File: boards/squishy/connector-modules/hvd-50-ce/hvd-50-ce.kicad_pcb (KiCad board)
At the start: 6 copper layers, 75 x 34 mm, 20 parts, among them J1 SCSI PHY Mezz, J3 Conn_01x04, J5 Centronics 50, U1 M24C02-RMC

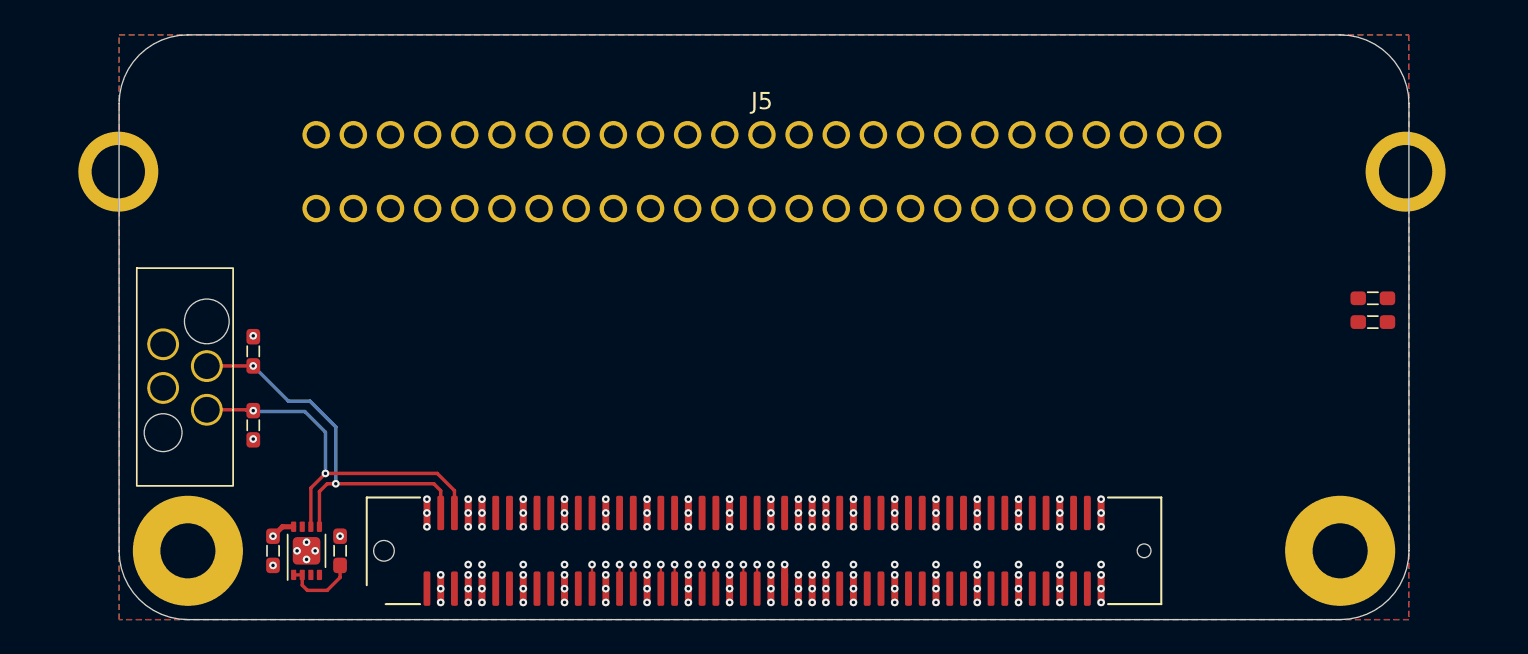
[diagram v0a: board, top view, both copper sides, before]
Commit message: squishy: connectors: added little earbs to the hvd-50-ce connector board
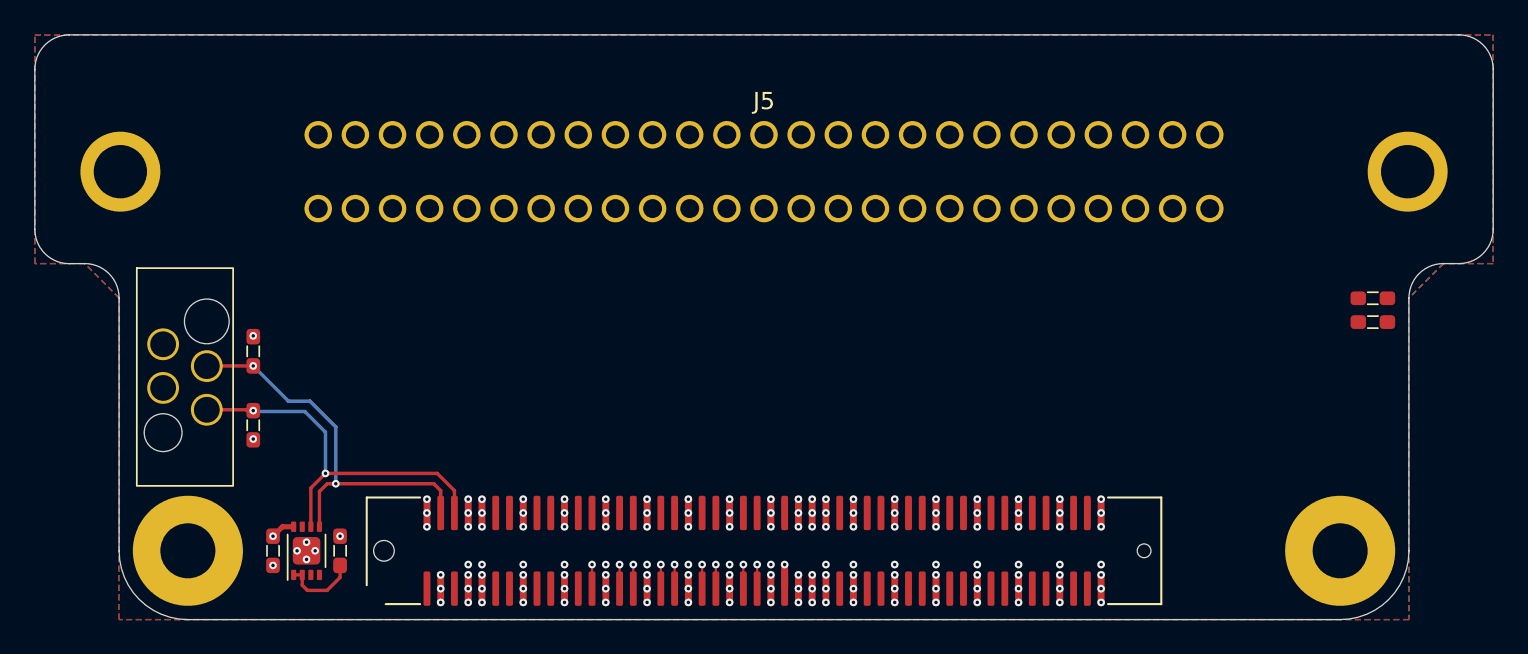
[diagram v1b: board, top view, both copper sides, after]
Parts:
- moved J5 0.12 mm to (147.5, 114.0)
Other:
- board size 75 x 34 mm -> 84.8 x 34 mm
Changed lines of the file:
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@@
 	(footprint "lethalbit-connectors:112-050-213R001"
 		(layer "F.Cu")
-		(at 147.38 113.955 180)
+		(at 147.5 113.955 180)
 		(descr "Norcomp 50-pin Centronics Connector")
 		(property "Reference" "J5"
@@
 	)
 	(gr_line
-		(start 181 106)
-		(end 114 106)
+		(start 187.9 106)
+		(end 107.1 106)
 		(locked yes)
 		(stroke
@@
 	)
 	(gr_arc
-		(start 110 110)
-		(mid 111.171573 107.171573)
-		(end 114 106)
+		(start 107.997502 119.297502)
+		(mid 109.413482 119.88402)
+		(end 110 121.3)
+		(locked yes)
+		(stroke
+			(width 0.05)
+			(type default)
+		)
+		(layer "Edge.Cuts")
+	)
+	(gr_line
+		(start 187 119.3)
+		(end 187.9 119.3)
 		(locked yes)
 		(stroke
@@
 	(gr_line
 		(start 185 136)
-		(end 185 110)
+		(end 185 121.3)
 		(locked yes)
 		(stroke
@@
 	)
 	(gr_arc
-		(start 181 106)
-		(mid 183.828427 107.171573)
-		(end 185 110)
+		(start 105.1 108.002498)
+		(mid 105.686517 106.586517)
+		(end 107.102498 106)
+		(locked yes)
+		(stroke
+			(width 0.05)
+			(type default)
+		)
+		(layer "Edge.Cuts")
+	)
+	(gr_arc
+		(start 107.102498 119.304996)
+		(mid 105.686517 118.718479)
+		(end 105.1 117.302498)
+		(locked yes)
+		(stroke
+			(width 0.05)
+			(type default)
+		)
+		(layer "Edge.Cuts")
+	)
+	(gr_arc
+		(start 185 121.3)
+		(mid 185.586518 119.88402)
+		(end 187.002498 119.297502)
 		(locked yes)
 		(stroke
@@
 	(gr_line
 		(start 110 136)
-		(end 110 110)
+		(end 110 121.3)
+		(locked yes)
+		(stroke
+			(width 0.05)
+			(type default)
+		)
+		(layer "Edge.Cuts")
+	)
+	(gr_line
+		(start 108 119.302498)
+		(end 107.1 119.302498)
+		(locked yes)
+		(stroke
+			(width 0.05)
+			(type default)
+		)
+		(layer "Edge.Cuts")
+	)
+	(gr_arc
+		(start 189.9 117.3)
+		(mid 189.313482 118.715981)
+		(end 187.897502 119.302498)
 		(locked yes)
 		(stroke
@@
 		(layer "Edge.Cuts")
 	)
+	(gr_arc
+		(start 187.897502 105.997502)
+		(mid 189.313483 106.584019)
+		(end 189.9 108)
+		(locked yes)
+		(stroke
+			(width 0.05)
+			(type default)
+		)
+		(layer "Edge.Cuts")
+	)
+	(gr_line
+		(start 189.9 117.3)
+		(end 189.9 108)
+		(locked yes)
+		(stroke
+			(width 0.05)
+			(type default)
+		)
+		(layer "Edge.Cuts")
+	)
+	(gr_line
+		(start 105.1 117.302498)
+		(end 105.1 108.002498)
+		(locked yes)
+		(stroke
+			(width 0.05)
+			(type default)
+		)
+		(layer "Edge.Cuts")
+	)
 	(gr_line
 		(start 23.5 34.517209)
@@
 		(polygon
 			(pts
-				(xy 185 140) (xy 110 140) (xy 110 106) (xy 185 106)
+				(xy 189.9 119.3) (xy 187 119.3) (xy 185 121.3) (xy 185 140) (xy 110 140) (xy 110 121.3) (xy 108 119.3)
+				(xy 105.1 119.3) (xy 105.1 106) (xy 189.9 106)
 			)
 		)
@@
 		(polygon
 			(pts
-				(xy 110 140) (xy 185 140) (xy 185 106) (xy 110 106)
+				(xy 105.1 119.3) (xy 108 119.3) (xy 110 121.3) (xy 110 140) (xy 185 140) (xy 185 121.3) (xy 187 119.3)
+				(xy 189.9 119.3) (xy 189.9 106) (xy 105.1 106)
 			)
 		)

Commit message: squishy: connectors: started routing on the hvd-50-ce
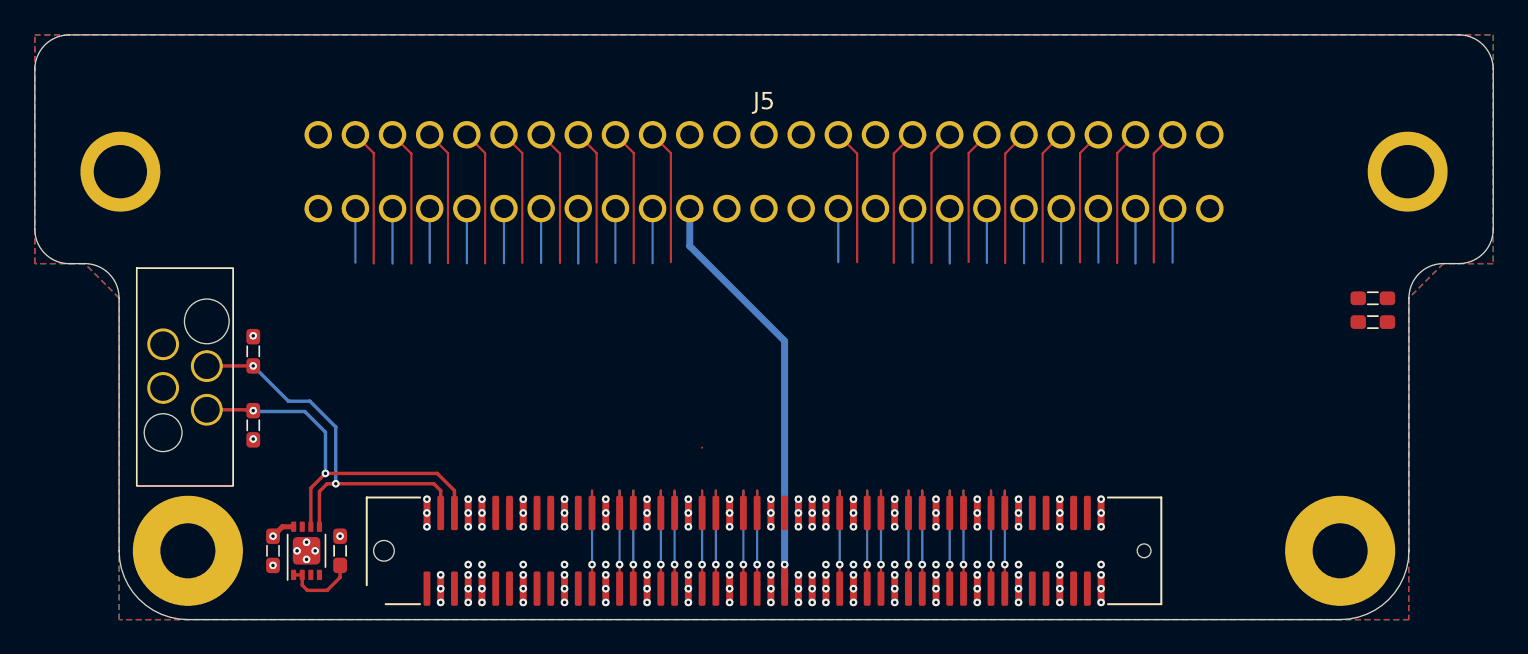
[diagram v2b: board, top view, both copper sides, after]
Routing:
- net /CON.DIFFSENSE: track 1.40 -> 24.4 mm
- net /CON.DB1-: track 0.00 -> 9.24 mm
- net /CON.DB0-: track 0.00 -> 9.23 mm
- net /CON.MSG-: track 0.00 -> 9.22 mm
- net /CON.DB3-: track 0.00 -> 9.21 mm
- net /CON.DB5-: track 0.00 -> 9.21 mm
- net /CON.DB2-: track 0.00 -> 9.21 mm
- net /CON.DB7-: track 0.00 -> 9.21 mm
- net /CON.BSY-: track 0.00 -> 9.20 mm
- net /CON.REQ-: track 0.00 -> 9.19 mm
- net /CON.ACK-: track 0.00 -> 9.19 mm
- net /CON.DB4-: track 0.00 -> 9.19 mm
- net /CON.I/O-: track 0.00 -> 9.18 mm
- net /CON.DB6-: track 0.00 -> 9.17 mm
- net /CON.ATN-: track 0.00 -> 9.16 mm
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
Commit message: squishy: connectors: Roughly routed out the hd-50-ce connector, still needs wiggles
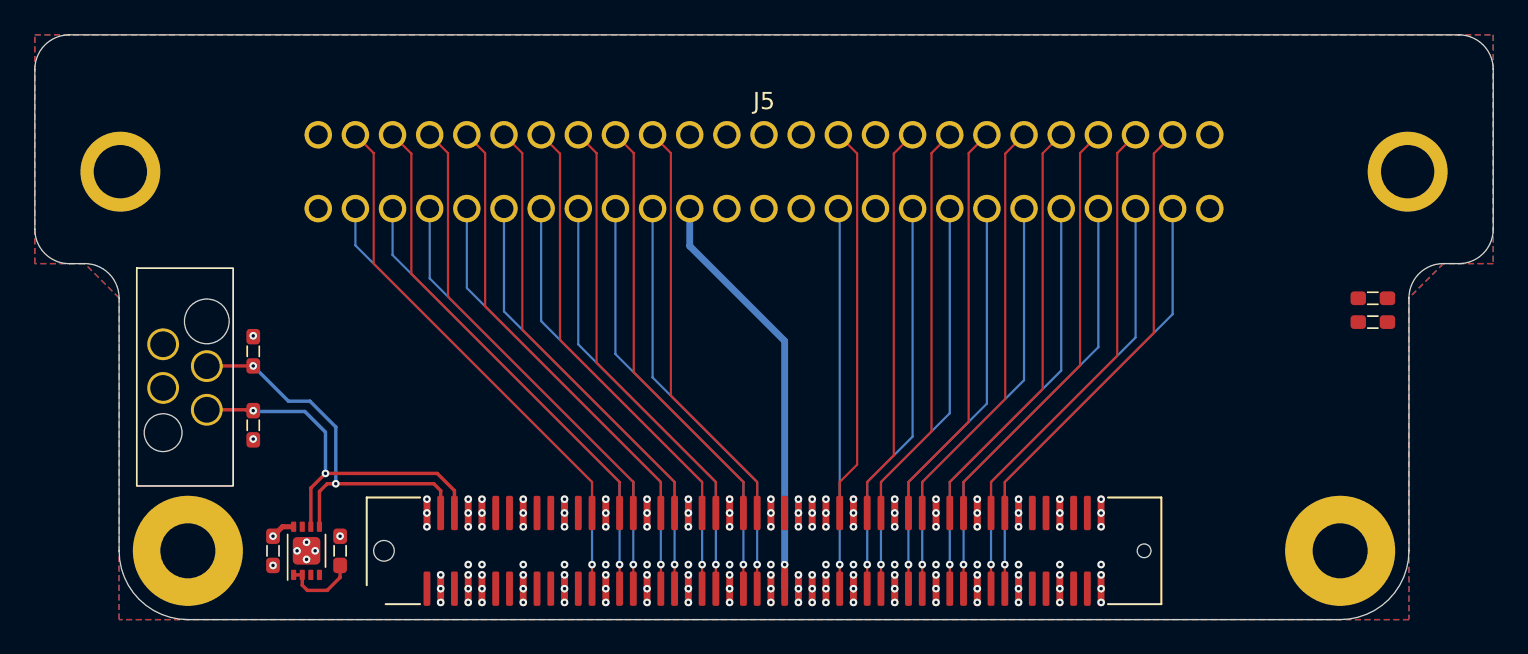
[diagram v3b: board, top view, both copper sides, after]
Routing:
- net /CON.DB0+: track 8.84 -> 27.8 mm
- net /CON.DB1+: track 8.90 -> 27.6 mm
- net /CON.DB0-: track 9.23 -> 27.7 mm
- net /CON.DB1-: track 9.24 -> 27.5 mm
- net /CON.DB2+: track 8.86 -> 27.0 mm
- net /CON.DB3+: track 8.88 -> 26.8 mm
- net /CON.DB2-: track 9.21 -> 26.9 mm
- net /CON.DB3-: track 9.21 -> 26.7 mm
- net /CON.DB4+: track 8.88 -> 26.2 mm
- net /CON.I/O+: track 8.84 -> 26.1 mm
- net /CON.DB5+: track 8.86 -> 26.0 mm
- net /CON.DB4-: track 9.19 -> 26.1 mm
- net /CON.I/O-: track 9.18 -> 26.0 mm
- net /CON.REQ+: track 8.90 -> 25.6 mm
- net /CON.DB5-: track 9.21 -> 25.9 mm
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
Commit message: squishy: connectors: added shield cap/resistor to hd-50-ce
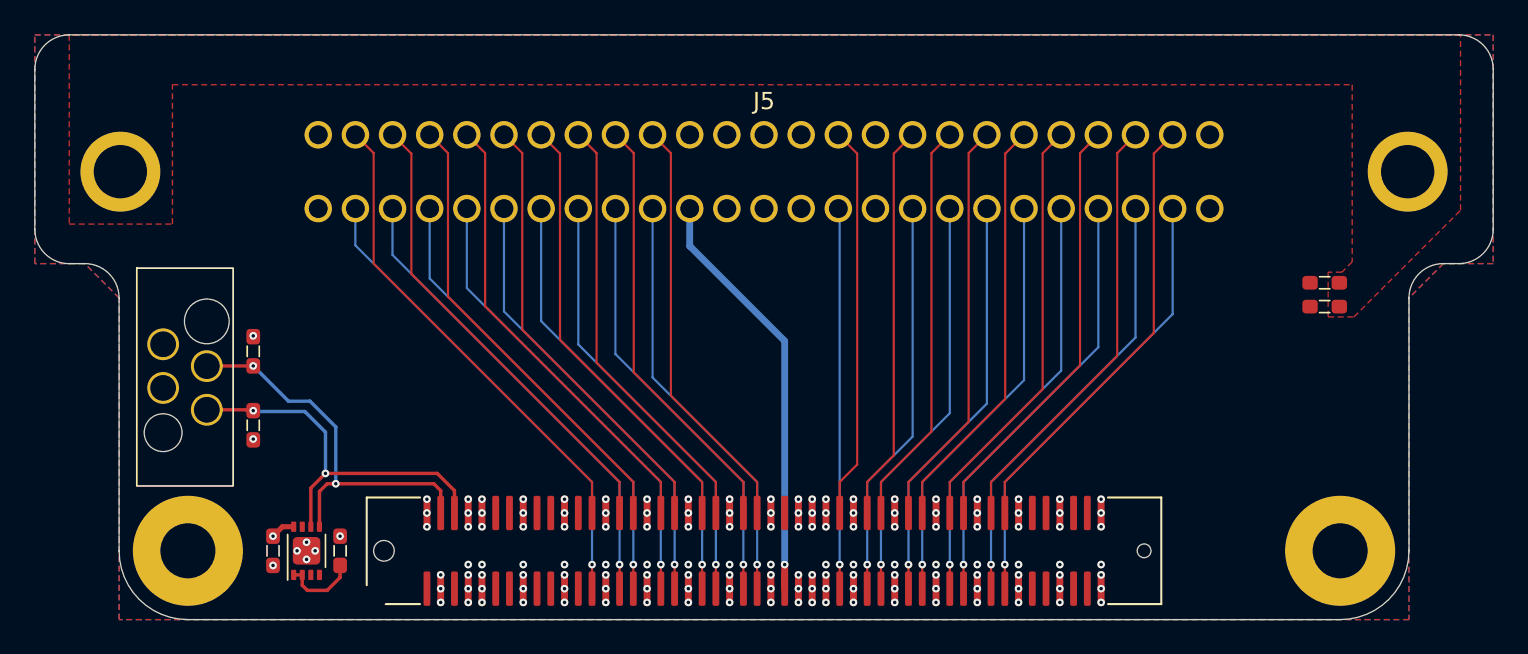
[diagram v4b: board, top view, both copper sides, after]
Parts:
- moved C2 3.61 mm to (180.1, 120.4), turned to 180 degrees
- moved R4 2.84 mm to (180.1, 121.8), turned to 0 degrees
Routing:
- added copper zone on F.Cu, net Net-(C2-Pad1)
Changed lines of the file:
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@@
 	(footprint "rhais_rcl:R0603"
 		(layer "F.Cu")
-		(at 182.9 121.315 180)
+		(at 180.1 121.8)
 		(descr "Ceramic Chip Resistor, 0603 (1608 metric) iron and air reflow solderable")
 		(property "Reference" "R4"
-			(at 0 1.315 0)
+			(at 0 1.314999 0)
 			(layer "F.Fab")
 			(effects
@@
 		)
 		(property "MFR" ""
-			(at 0 0 180)
+			(at 0 0 0)
 			(unlocked yes)
 			(layer "F.Fab")
@@
 		)
 		(property "MPN" ""
-			(at 0 0 180)
+			(at 0 0 0)
 			(unlocked yes)
 			(layer "F.Fab")
@@
 		)
 		(property "Tolerance" ""
-			(at 0 0 180)
+			(at 0 0 0)
 			(unlocked yes)
 			(layer "F.Fab")
@@
 		)
 		(property "SUPPLIER" "DigiKey"
-			(at 0 0 180)
+			(at 0 0 0)
 			(unlocked yes)
 			(layer "F.Fab")
@@
 		)
 		(property "SUPPLIER_OC" ""
-			(at 0 0 180)
+			(at 0 0 0)
 			(unlocked yes)
 			(layer "F.Fab")
@@
 		)
 		(property "SUPPLIER_URL" ""
-			(at 0 0 180)
+			(at 0 0 0)
 			(unlocked yes)
 			(layer "F.Fab")
@@
 		)
 		(fp_line
-			(start 0.3 -0.349999)
-			(end -0.3 -0.349999)
+			(start -0.3 0.349999)
+			(end 0.3 0.349999)
 			(stroke
 				(width 0.1)
@@
 		)
 		(fp_line
-			(start -0.3 0.349999)
-			(end 0.3 0.349999)
+			(start 0.3 -0.349999)
+			(end -0.3 -0.349999)
 			(stroke
 				(width 0.1)
@@
 		)
 		(fp_line
-			(start 1.55 0.65)
-			(end -1.55 0.65)
+			(start -1.55 -0.65)
+			(end 1.55 -0.65)
 			(stroke
 				(width 0.05)
@@
 		)
 		(fp_line
-			(start 1.55 -0.65)
-			(end 1.55 0.65)
+			(start -1.55 0.65)
+			(end -1.55 -0.65)
 			(stroke
 				(width 0.05)
@@
 		)
 		(fp_line
-			(start -1.55 0.65)
-			(end -1.55 -0.65)
+			(start 1.55 -0.65)
+			(end 1.55 0.65)
 			(stroke
 				(width 0.05)
@@
 		)
 		(fp_line
-			(start -1.55 -0.65)
-			(end 1.55 -0.65)
+			(start 1.55 0.65)
+			(end -1.55 0.65)
 			(stroke
 				(width 0.05)
@@
 		)
 		(fp_line
-			(start 0.45 -0.349999)
-			(end -0.45 -0.349999)
+			(start -0.45 0.349999)
+			(end 0.45 0.349999)
 			(stroke
 				(width 0.1)
@@
 		)
 		(fp_line
-			(start -0.45 0.349999)
-			(end 0.45 0.349999)
+			(start 0.45 -0.349999)
+			(end -0.45 -0.349999)
 			(stroke
 				(width 0.1)
@@
 		(fp_poly
 			(pts
-				(xy 0.4 0.4) (xy 0.8 0.4) (xy 0.8 -0.4) (xy 0.4 -0.4)
+				(xy -0.8 0.4) (xy -0.4 0.4) (xy -0.4 -0.4) (xy -0.8 -0.4)
 			)
 			(stroke
@@
 		(fp_poly
 			(pts
-				(xy -0.8 0.4) (xy -0.4 0.4) (xy -0.4 -0.4) (xy -0.8 -0.4)
+				(xy 0.4 0.4) (xy 0.8 0.4) (xy 0.8 -0.4) (xy 0.4 -0.4)
 			)
 			(stroke
@@
 		)
 		(pad "1" smd roundrect
-			(at -0.85 0 180)
+			(at -0.85 0)
 			(size 0.9 0.8)
 			(layers "F.Cu" "F.Paste" "F.Mask")
@@
 		)
 		(pad "2" smd roundrect
-			(at 0.85 0 180)
+			(at 0.85 0)
 			(size 0.9 0.8)
 			(layers "F.Cu" "F.Paste" "F.Mask")
@@
 	)
 	(footprint "lethalbit-connectors:112-050-213R001"
+		(locked yes)
 		(layer "F.Cu")
 		(at 147.5 113.955 180)
@@
 	(footprint "rhais_rcl:C0603"
 		(layer "F.Cu")
-		(at 182.9 122.7)
+		(at 180.1 120.415 180)
 		(descr "Multi-Layer Ceramic Chip Capacitor, 0603 (1608 metric) iron and air reflow solderable")
 		(property "Reference" "C2"
@@
 		)
 		(property "MFR" "KEMET"
-			(at 0 0 0)
+			(at 0 0 180)
 			(unlocked yes)
 			(layer "F.Fab")
@@
 		)
 		(property "MPN" "C0603C104M5RACTU"
-			(at 0 0 0)
+			(at 0 0 180)
 			(unlocked yes)
 			(layer "F.Fab")
@@
 		)
 		(property "Tolerance" "±20% 50V"
-			(at 0 0 0)
+			(at 0 0 180)
 			(unlocked yes)
 			(layer "F.Fab")
@@
 		)
 		(property "SUPPLIER" "DigiKey"
-			(at 0 0 0)
+			(at 0 0 180)
 			(unlocked yes)
 			(layer "F.Fab")
@@
 		)
 		(property "SUPPLIER_OC" "399-C0603C104M5RAC7867DKR-ND"
-			(at 0 0 0)
+			(at 0 0 180)
 			(unlocked yes)
 			(layer "F.Fab")
@@
 		)
 		(property "SUPPLIER_URL" "https://www.digikey.com/short/8nqzrr4b"
-			(at 0 0 0)
+			(at 0 0 180)
 			(unlocked yes)
 			(layer "F.Fab")
@@
 		)
 		(fp_line
-			(start -0.3 -0.349999)
-			(end 0.3 -0.349999)
+			(start 0.3 0.349999)
+			(end -0.3 0.349999)
 			(stroke
 				(width 0.1)
@@
 		)
 		(fp_line
-			(start 0.3 0.349999)
-			(end -0.3 0.349999)
+			(start -0.3 -0.349999)
+			(end 0.3 -0.349999)
 			(stroke
 				(width 0.1)
@@
 		)
 		(fp_line
-			(start -1.55 -0.65)
-			(end -1.55 0.65)
+			(start 1.55 0.65)
+			(end 1.55 -0.65)
 			(stroke
 				(width 0.05)
@@
 		)
 		(fp_line
-			(start -1.55 0.65)
-			(end 1.55 0.65)
+			(start 1.55 -0.65)
+			(end -1.55 -0.65)
 			(stroke
 				(width 0.05)
@@
 		)
 		(fp_line
-			(start 1.55 -0.65)
-			(end -1.55 -0.65)
+			(start -1.55 0.65)
+			(end 1.55 0.65)
 			(stroke
 				(width 0.05)
@@
 		)
 		(fp_line
-			(start 1.55 0.65)
-			(end 1.55 -0.65)
+			(start -1.55 -0.65)
+			(end -1.55 0.65)
 			(stroke
 				(width 0.05)
@@
 		)
 		(fp_line
-			(start -0.45 -0.349999)
-			(end 0.45 -0.349999)
+			(start -0.45 0.349999)
+			(end 0.45 0.349999)
 			(stroke
 				(width 0.1)
@@
 		)
 		(fp_line
-			(start -0.45 0.349999)
-			(end 0.45 0.349999)
+			(start -0.45 -0.349999)
+			(end 0.45 -0.349999)
 			(stroke
 				(width 0.1)
@@
 		(fp_poly
 			(pts
-				(xy -0.8 0.4) (xy -0.4 0.4) (xy -0.4 -0.4) (xy -0.8 -0.4)
+				(xy 0.4 0.4) (xy 0.8 0.4) (xy 0.8 -0.4) (xy 0.4 -0.4)
 			)
 			(stroke
@@
 		(fp_poly
 			(pts
-				(xy 0.4 0.4) (xy 0.8 0.4) (xy 0.8 -0.4) (xy 0.4 -0.4)
+				(xy -0.8 0.4) (xy -0.4 0.4) (xy -0.4 -0.4) (xy -0.8 -0.4)
 			)
 			(stroke
@@
 		)
 		(pad "1" smd roundrect
-			(at -0.85 0)
+			(at -0.85 0 180)
 			(size 0.9 0.8)
 			(layers "F.Cu" "F.Paste" "F.Mask")
@@
 		)
 		(pad "2" smd roundrect
-			(at 0.85 0)
+			(at 0.85 0 180)
 			(size 0.9 0.8)
 			(layers "F.Cu" "F.Paste" "F.Mask")
@@
 	)
 	(zone
+		(net 64)
+		(net_name "Net-(C2-Pad1)")
+		(layer "F.Cu")
+		(hatch edge 0.5)
+		(priority 3)
+		(connect_pads yes
+			(clearance 0.2)
+		)
+		(min_thickness 0.1)
+		(filled_areas_thickness no)
+		(fill yes
+			(thermal_gap 0.2)
+			(thermal_bridge_width 0.4)
+			(smoothing fillet)
+			(radius 0.2)
+		)
+		(polygon
+			(pts
+				(xy 181.7 119.2) (xy 181.1 119.8) (xy 180.3 119.8) (xy 180.3 122.4) (xy 181.8 122.4) (xy 188 116.2)
+				(xy 188 106) (xy 107.1 106) (xy 107.1 117) (xy 113.1 117) (xy 113.1 108.9) (xy 181.7 108.9)
+			)
+		)
+	)
+	(zone

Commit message: squishy: connectors: ensured the hd-50-ce connector was routed and updated the KiKit tab symbols
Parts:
- J5: value Centronics 50 -> 112-050-213R001
- moved REF** 4.65 mm to (189.9, 115.0)
- moved REF** 4.60 mm to (105.1, 115.0)
- moved REF** 0.30 mm to (110.0, 131.0)
- moved REF** 0.25 mm to (121.0, 106.0)
- moved REF** 0.25 mm to (185.0, 131.0)
- moved REF** 0.25 mm to (174.0, 140.0)
- moved REF** 0.25 mm to (174.0, 106.0)
- moved REF** 0.25 mm to (121.0, 140.0)
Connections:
- net /CON.DP12+ renamed /CON.DB12+
- net /CON.DP12- renamed /CON.DB12-
- net /CON.DP14+ renamed /CON.DB14+
- net /CON.DP14- renamed /CON.DB14-
